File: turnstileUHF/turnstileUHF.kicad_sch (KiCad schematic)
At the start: 54 parts, among them J5 RFPC-SMA28-F, Q1 2N7002, Q2 2N7002, Q3 2N7002, Q4 2N7002, Q5 AO3401A, Q6 AO3401A, Q7 AO3401A, Q8 2N7002, U1 74HCT238D

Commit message: door sensing not update?
tryint to push changes
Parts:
- added C1: 10 nF, Capacitor_SMD:C_0603_1608Metric, symbol Device:C
- added C2, C3: 100 nF, Capacitor_SMD:C_0603_1608Metric, symbol Device:C
- added J2: Conn_01x04, Connector_JST:JST_PH_S4B-PH-K_1x04_P2.00mm_Horizontal, symbol Connector_Generic:Conn_01x04
- added J3: Conn_01x02, Connector_JST:JST_PH_S2B-PH-K_1x02_P2.00mm_Horizontal, symbol Connector_Generic:Conn_01x02
- added R1, R3: 1k, Resistor_SMD:R_0603_1608Metric, symbol Device:R_US
- added R2: 64.9k, Resistor_SMD:R_0603_1608Metric, symbol Device:R_US
- added U2: ADS1015IDGSR, ADS1115:DGS0010A_M, symbol ADS1115:ADS1115IDGSR
- added U3: OPA333xxD, Package_SO:SOIC-8_3.9x4.9mm_P1.27mm, symbol Amplifier_Operational:OPA333xxD
- added U4: TPD1E05U06DYA, Diode_SMD:D_SOD-523, symbol Power_Protection:TPD1E05U06DYA
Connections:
- net GND: now also C1.2, C2.1, C3.2, J2.2 (Pin_2), U2.1 (ADDR), U2.3 (GND), U2.6 (AIN2), U2.7 (AIN3), U3.4 (V-), U4.2 (GND)
- new net: J3.2 (Pin_2), R1.1, R2.2, U4.1 (I/O)
- new net: C1.1, R1.2, U3.3 (+)
- new net: U2.4 (AIN0), U3.2 (-), U3.6
- new net: J2.4 (Pin_4), U2.10 (SCL)
- new net: R3.1, U2.5 (AIN1)
- new net: J2.3 (Pin_3), U2.9 (SDA)
- new net 3.3V: C2.2, C3.1, J2.1 (Pin_1), R2.1, R3.2, U2.8 (VDD), U3.7 (V+)
- no-connect marks 4 -> 5
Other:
- note added: "I/O Flight Controller"
- moved on the sheet: Burn1, Burn2, Burn3, Burn4, Q1, Q2, Q3, Q4, Q5, Q6, Q7, Q8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

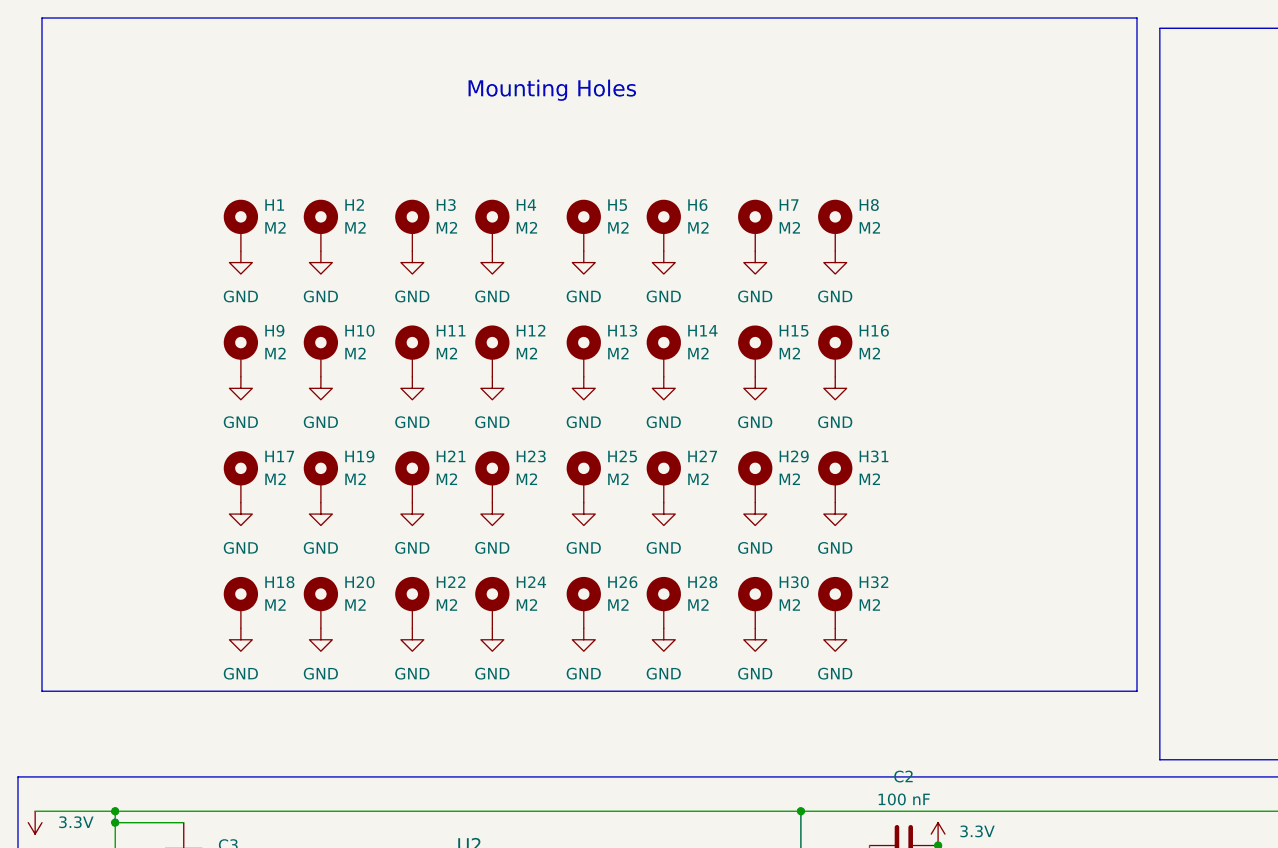
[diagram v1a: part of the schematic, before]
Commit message: integrated door sensing into schematic
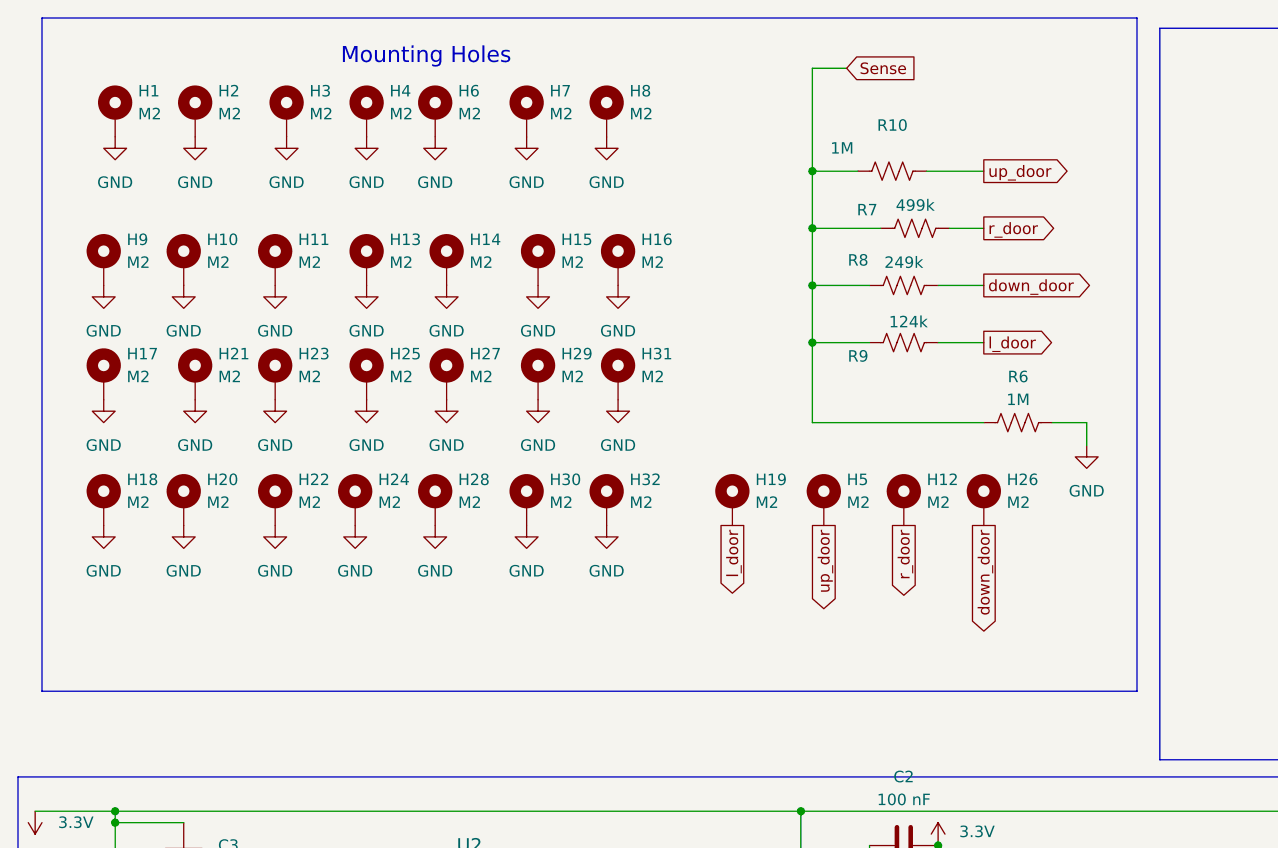
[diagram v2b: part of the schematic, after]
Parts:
- added R10, R6: 1M, Resistor_SMD:R_0603_1608Metric, symbol Device:R_US
- added R7: 499k, Resistor_SMD:R_0603_1608Metric, symbol Device:R_US
- added R8: 249k, Resistor_SMD:R_0603_1608Metric, symbol Device:R_US
- added R9: 124k, Resistor_SMD:R_0603_1608Metric, symbol Device:R_US
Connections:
- net GND: now also R6.2; no longer H12.1, H19.1, H26.1, H5.1
- new net Sense: R10.1, R6.1, R7.1, R8.1, R9.1
- new net down_door: H26.1, R8.2
- new net l_door: H19.1, R9.2
- new net r_door: H12.1, R7.2
- new net up_door: H5.1, R10.2
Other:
- moved on the sheet: H1, H10, H11, H12, H13, H14, H15, H16, H17, H18, H19, H2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

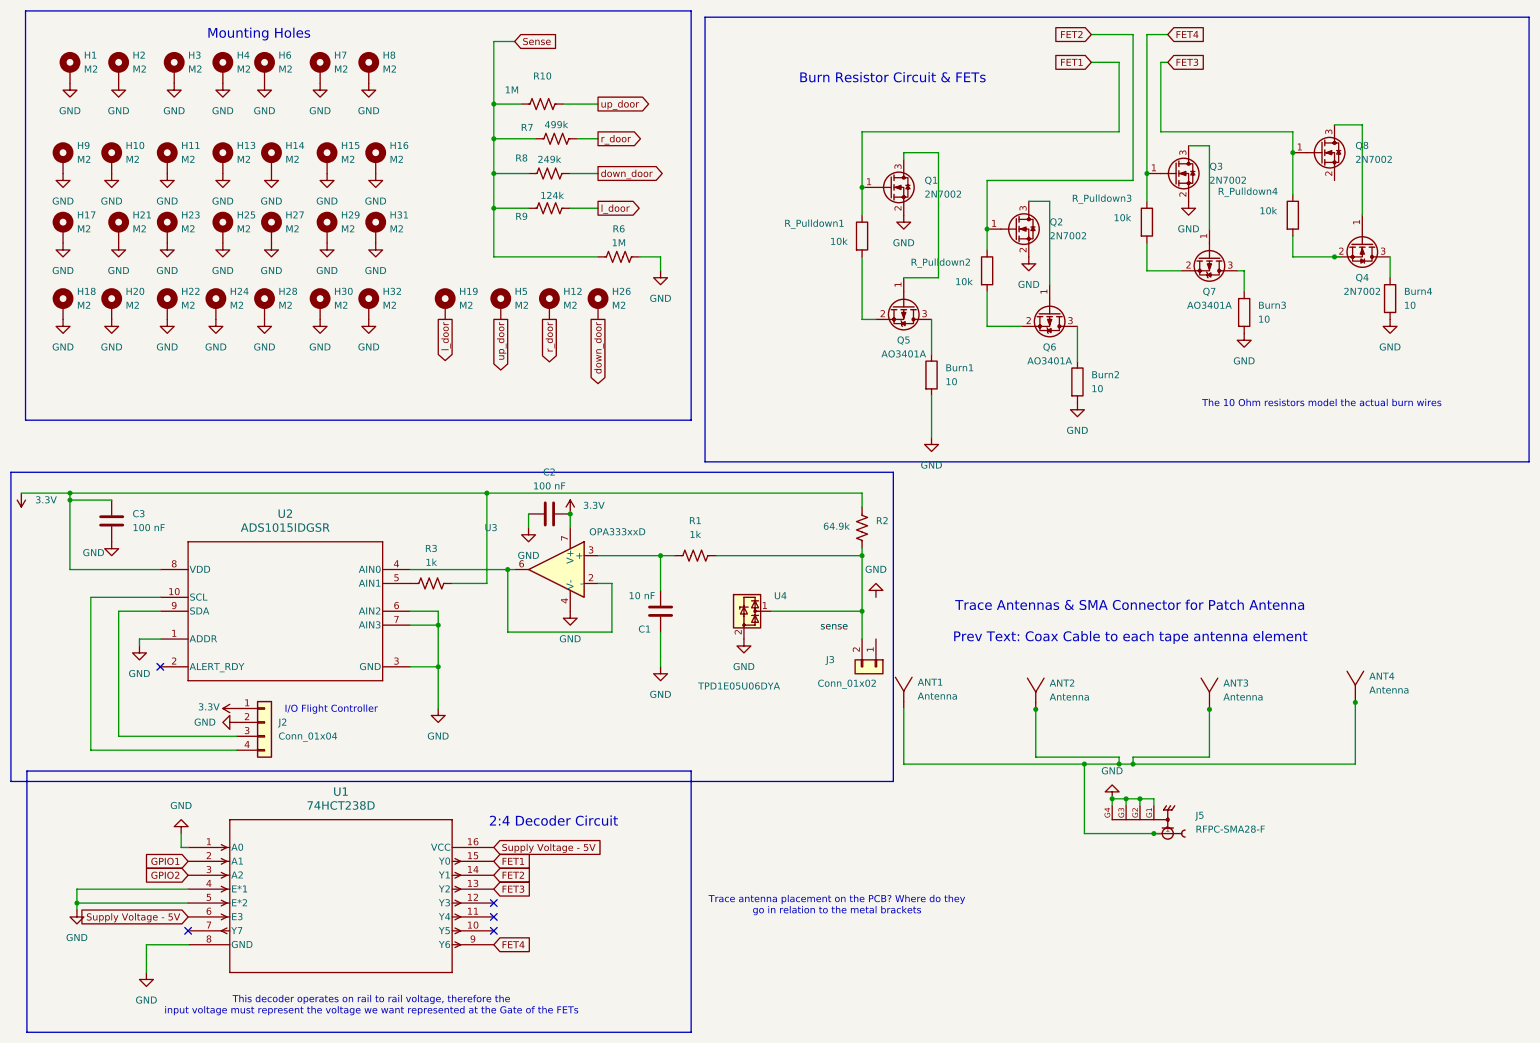
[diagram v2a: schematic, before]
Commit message: switched added to schematic
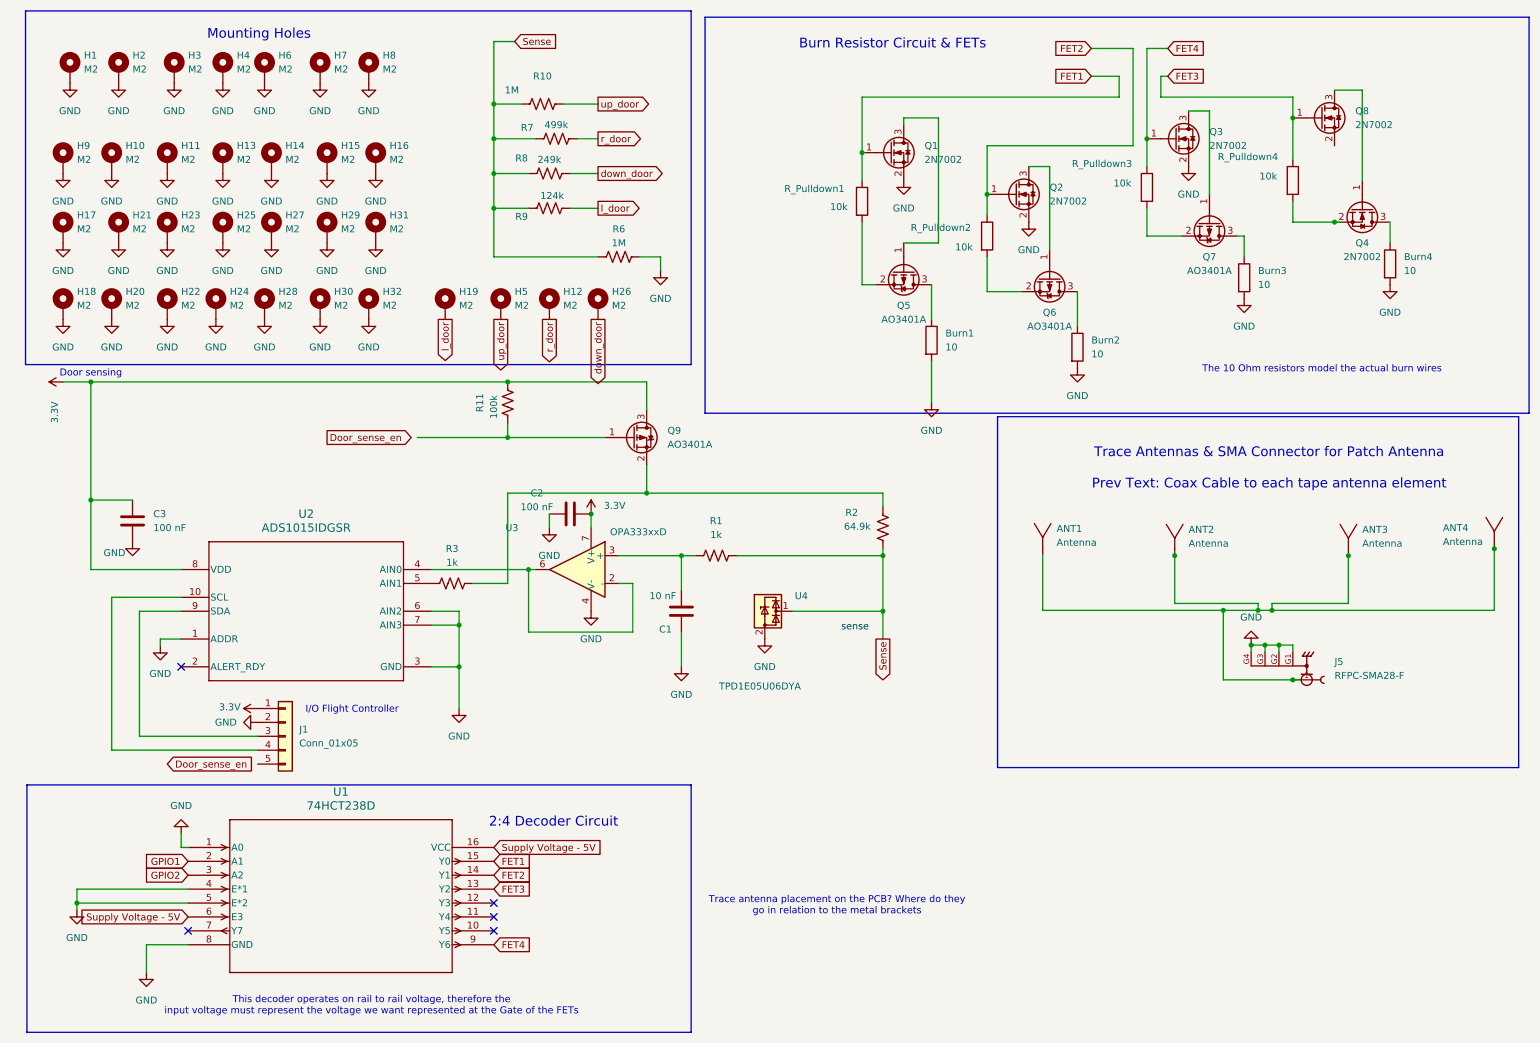
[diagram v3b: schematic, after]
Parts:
- removed J2: Conn_01x04, Connector_JST:JST_PH_S4B-PH-K_1x04_P2.00mm_Horizontal, symbol Connector_Generic:Conn_01x04
- removed J3: Conn_01x02, Connector_JST:JST_PH_S2B-PH-K_1x02_P2.00mm_Horizontal, symbol Connector_Generic:Conn_01x02
- added J1: Conn_01x05, symbol Connector_Generic:Conn_01x05
- added Q9: AO3401A, Package_TO_SOT_SMD:SOT-23, symbol Transistor_FET:AO3401A
- added R11: 100k, Resistor_SMD:R_0603_1608Metric, symbol Device:R_US
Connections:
- net 3.3V: now also J1.1 (Pin_1), Q9.3 (D), R11.2; no longer R2.1, R3.2
- net GND: now also J1.2 (Pin_2)
- net Sense: now also R1.1, R2.2, U4.1 (I/O)
- net at U2.10 (SCL): now also J1.4 (Pin_4)
- net at U2.9 (SDA): now also J1.3 (Pin_3)
- new net: Q9.1 (G), R11.1
- new net: Q9.2 (S), R2.1, R3.2
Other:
- note added: "Door sensing"
- moved on the sheet: ANT1, ANT2, ANT3, ANT4, Burn1, Burn2, Burn3, Burn4, C1, C2, C3, J5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
